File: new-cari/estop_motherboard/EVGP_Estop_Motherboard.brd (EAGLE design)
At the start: 82.6 x 94.1 mm, 45 parts, among them J1 JST-XH-02-PIN-LONG-PAD, J2 JST-XH-02-PIN-LONG-PAD, J3 JST-XH-03-PIN-LONG-PAD, J4 JST-XH-03-PIN-LONG-PAD, J5 AVR_SPI_PROG_3X2PTH, J6 UX60-MB-5S8, J7 JST-XH-04-PIN-LONG-PAD, J8 JST-XH-03-PIN-LONG-PAD, J9 JST-XH-02-PIN-LONG-PAD, Q1 NFETS_1, Q2 N_FETS2, U1 ATMEGA32U4-AU, U2 NL27WZ08USG, U3 NL27WZ08USG, X1 TSX-3225 16.0000MF18X-AC0

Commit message: test
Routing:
- net PUSH_BUTTON: track 32.5 -> 28.5 mm
- net STEERING_EN_OUT: track 28.5 -> 26.2 mm
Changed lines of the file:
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@@
 <?xml version="1.0" encoding="utf-8"?>
 <!DOCTYPE eagle SYSTEM "eagle.dtd">
-<eagle version="9.5.0">
+<eagle version="9.5.1">
 <drawing>
 <settings>
-<setting alwaysvectorfont="no"/>
+<setting alwaysvectorfont="yes"/>
 <setting verticaltext="up"/>
 </settings>
@@
 <wire x1="66.1966" y1="7.08" x2="68" y2="8.8834" width="0.2032" layer="1"/>
 <via x="68" y="8.8834" extent="1-16" drill="0.508"/>
-<via x="72.022303125" y="11.922303125" extent="1-16" drill="0.508"/>
-<wire x1="68" y1="8.8834" x2="71.038903125" y2="11.922303125" width="0.2032" layer="16"/>
-<wire x1="71.038903125" y1="11.922303125" x2="72.022303125" y2="11.922303125" width="0.2032" layer="16"/>
+<via x="72.622303125" y="11.722303125" extent="1-16" drill="0.508"/>
+<wire x1="68" y1="8.8834" x2="70.838903125" y2="11.722303125" width="0.2032" layer="16"/>
+<wire x1="70.838903125" y1="11.722303125" x2="72.622303125" y2="11.722303125" width="0.2032" layer="16"/>
 <wire x1="76.9224" y1="9.25" x2="76.31118125" y2="9.25" width="0.2032" layer="1"/>
-<wire x1="73.638878125" y1="11.922303125" x2="72.022303125" y2="11.922303125" width="0.2032" layer="1"/>
-<wire x1="76.31118125" y1="9.25" x2="73.638878125" y2="11.922303125" width="0.2032" layer="1"/>
+<wire x1="73.838878125" y1="11.722303125" x2="72.622303125" y2="11.722303125" width="0.2032" layer="1"/>
+<wire x1="76.31118125" y1="9.25" x2="73.838878125" y2="11.722303125" width="0.2032" layer="1"/>
 </signal>
 <signal name="STEERING_EN_RB">
@@
 <wire x1="80.5" y1="17.95" x2="81.65" y2="19.1" width="0.2032" layer="1"/>
 <wire x1="80.5" y1="11.79746875" x2="80.5" y2="17.95" width="0.2032" layer="1"/>
-<wire x1="80.55" y1="22.05" x2="80.55" y2="20.2" width="0.2032" layer="1"/>
-<wire x1="81.65" y1="19.1" x2="80.55" y2="20.2" width="0.2032" layer="1"/>
-<wire x1="81.5" y1="23" x2="86" y2="23" width="0.2032" layer="1"/>
-<wire x1="86" y1="23" x2="87" y2="24" width="0.2032" layer="1"/>
-<wire x1="87" y1="26.5" x2="85.53" y2="27.97" width="0.2032" layer="1"/>
+<wire x1="86.5" y1="27" x2="86.5" y2="23.95" width="0.2032" layer="1"/>
+<wire x1="81.65" y1="19.1" x2="86.5" y2="23.95" width="0.2032" layer="1"/>
+<wire x1="86.5" y1="27" x2="85.53" y2="27.97" width="0.2032" layer="1"/>
 <wire x1="85.53" y1="27.97" x2="84.4" y2="27.97" width="0.2032" layer="1"/>
-<wire x1="80.55" y1="22.05" x2="81.5" y2="23" width="0.2032" layer="1"/>
-<wire x1="87" y1="24" x2="87" y2="26.5" width="0.2032" layer="1"/>
 </signal>
 <signal name="DRIVE_EN_OUT">
@@
 <contactref element="U2" pad="3"/>
 <contactref element="J1" pad="1"/>
-<wire x1="84.5" y1="1.23" x2="80.77" y2="1.23" width="0.2032" layer="1"/>
-<wire x1="80" y1="6" x2="79.5" y2="6.5" width="0.2032" layer="1"/>
-<wire x1="80.77" y1="1.23" x2="80" y2="2" width="0.2032" layer="1"/>
-<wire x1="80" y1="2" x2="80" y2="6" width="0.2032" layer="1"/>
+<wire x1="84.5" y1="1.23" x2="78.07" y2="1.23" width="0.2032" layer="1"/>
+<wire x1="78.07" y1="1.23" x2="71.3" y2="8" width="0.2032" layer="1"/>
 <wire x1="70.2" y1="10.46118125" x2="70.2" y2="13.2" width="0.2032" layer="1"/>
 <via x="70.2" y="13.2" extent="1-16" drill="0.508"/>
-<wire x1="72.8" y1="6.5" x2="71.3" y2="8" width="0.2032" layer="1"/>
 <wire x1="71.3" y1="8" x2="71.3" y2="9.4" width="0.2032" layer="1"/>
 <wire x1="71.3" y1="9.4" x2="70.2" y2="10.46118125" width="0.2032" layer="1"/>
@@
 <wire x1="74.0776" y1="14.75" x2="71.905390625" y2="14.75" width="0.2032" layer="1"/>
 <wire x1="71.877696875" y1="14.722303125" x2="71.905390625" y2="14.75" width="0.2032" layer="1"/>
-<wire x1="79.5" y1="6.5" x2="72.8" y2="6.5" width="0.2032" layer="1"/>
 </signal>
 <signal name="STEERING_EN_IN">

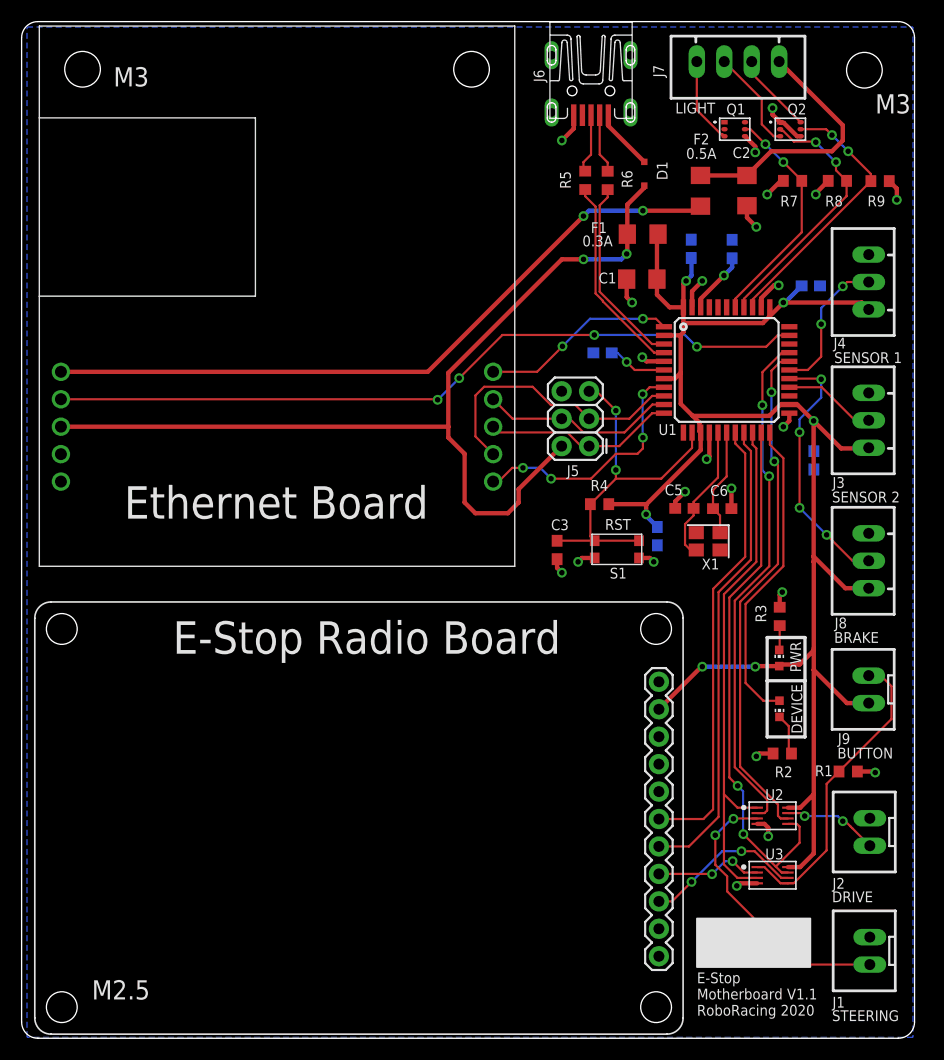
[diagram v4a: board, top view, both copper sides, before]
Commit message: updated ethernet poe board, made some minor rerouting changes, and cleaned everything up a bit
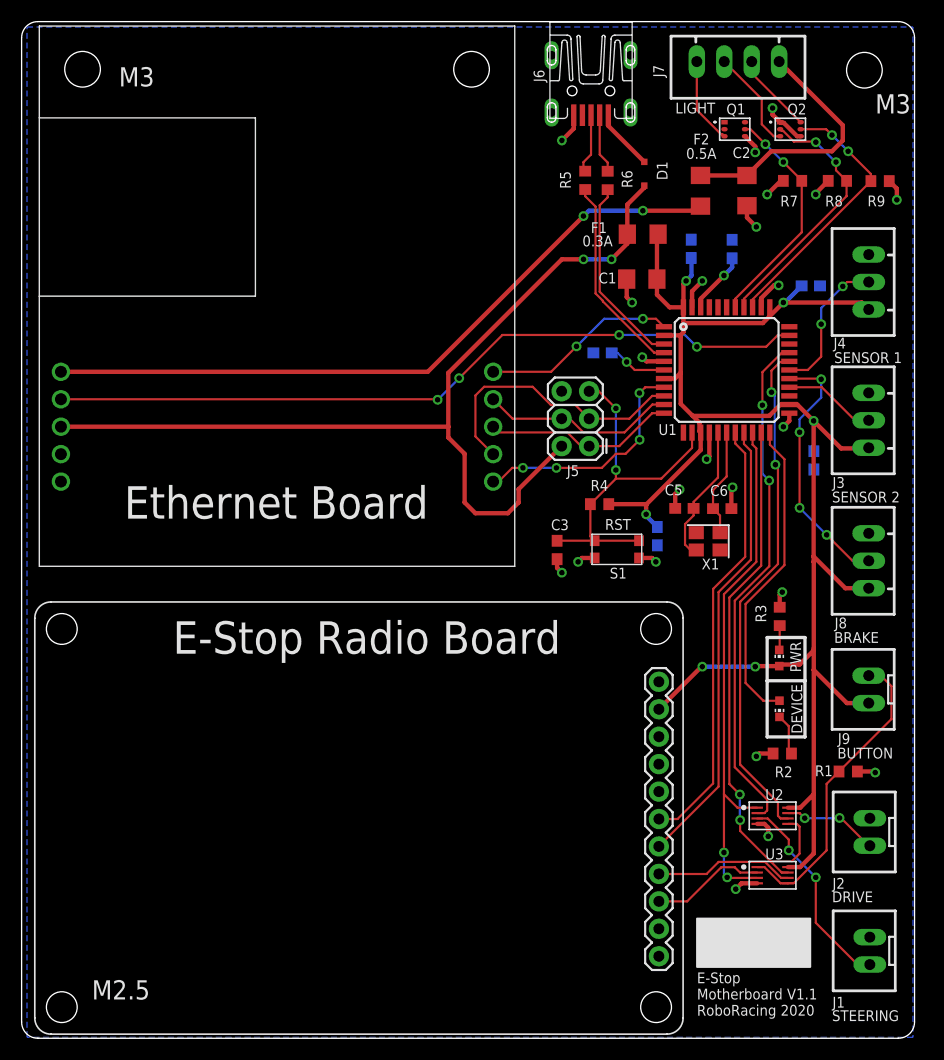
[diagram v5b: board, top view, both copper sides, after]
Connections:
- net DRIVE_EN_RB: now also U3.2; no longer U3.6
- net STEERING_EN_RB: now also U3.6; no longer U3.2
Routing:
- net STEERING_EN_OUT: track 26.2 -> 19.1 mm
- net DRIVE_EN_RB: track 14.9 -> 10.6 mm, vias 2 -> 0
- net STEERING_EN_RB: track 10.0 -> 13.0 mm, vias 2 -> 0
- net START_RB: track 43.7 -> 42.1 mm
- net SAFE_RB: track 41.9 -> 40.5 mm
- net SS: track 23.2 -> 22.0 mm
- net DRIVE_EN_IN: track 50.3 -> 51.2 mm
- net GND: track 48.4 -> 49.0 mm
- net STEERING_EN_IN: track 48.5 -> 49.1 mm, vias 0 -> 2
- net 5V_UNFUSED: track 89.2 -> 88.7 mm

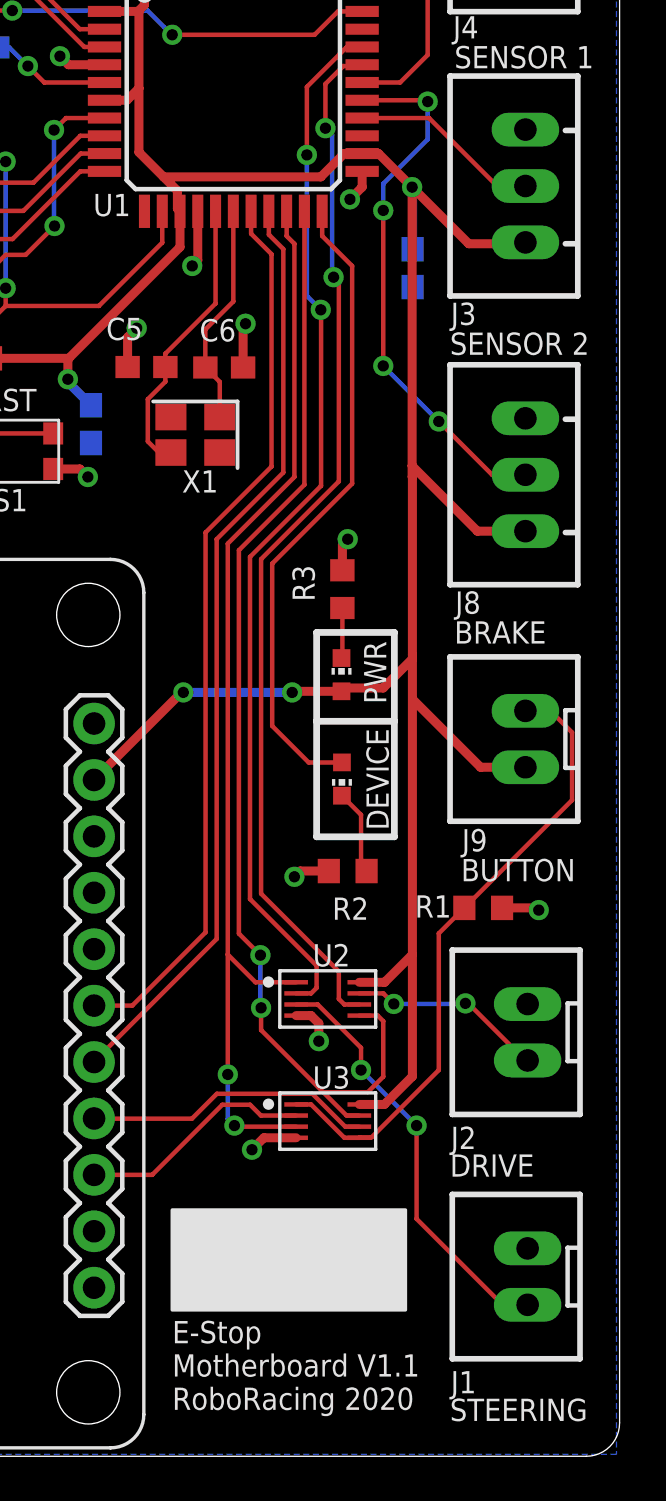
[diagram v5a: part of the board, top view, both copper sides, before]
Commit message: moved LED1 to pin 25
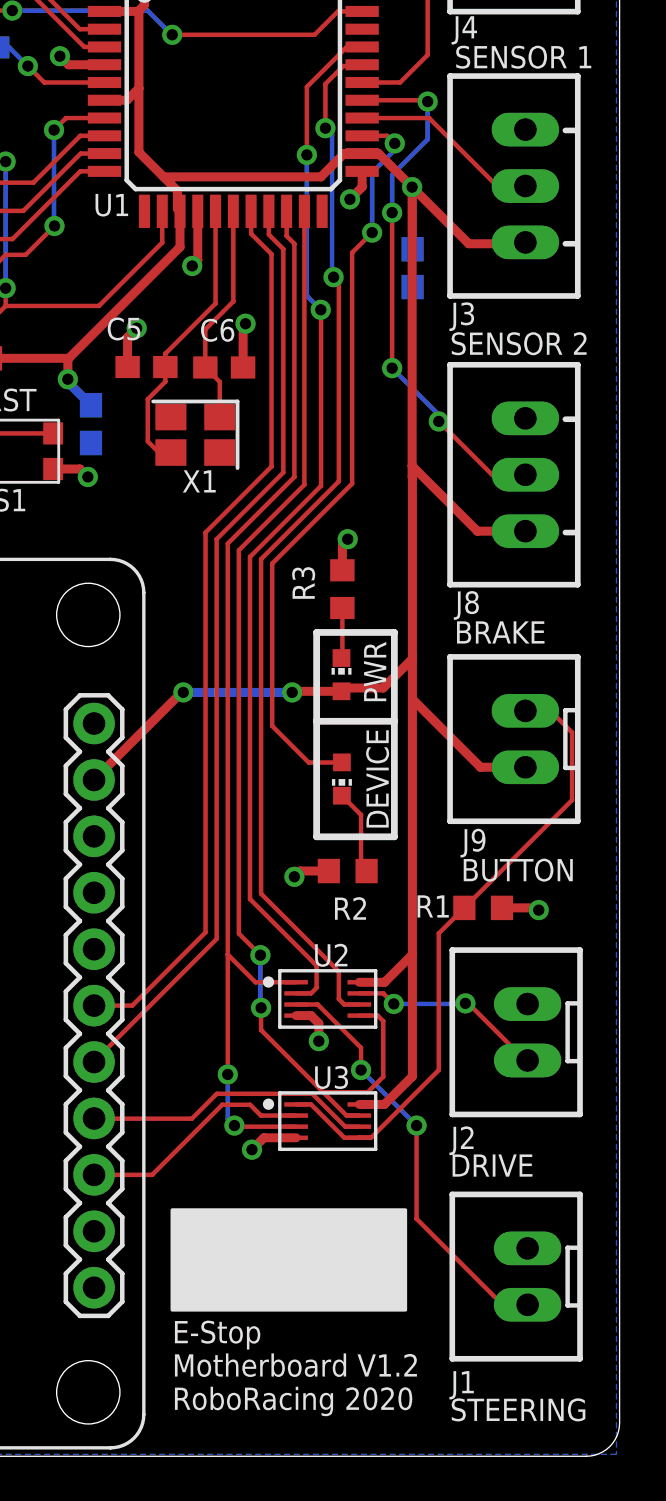
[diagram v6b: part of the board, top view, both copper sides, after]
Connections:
- net LED1: now also U1.25; no longer U1.22
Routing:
- net LED1: track 29.0 -> 33.9 mm, vias 0 -> 2
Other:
- board text added: "E-Stop Motherboard V1.2 RoboRacing 2020"
- board text removed: "E-Stop Motherboard V1.1 RoboRacing 2020"
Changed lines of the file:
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@@
 <drawing>
 <settings>
-<setting alwaysvectorfont="yes"/>
+<setting alwaysvectorfont="no"/>
 <setting verticaltext="up"/>
 </settings>
@@
 <text x="67.5" y="75.8" size="1" layer="21" font="vector">0.5A</text>
 <text x="68.5" y="-3.5" size="1" layer="21" font="vector">E-Stop
-Motherboard V1.1
+Motherboard V1.2
 RoboRacing 2020</text>
 <polygon width="0.1524" layer="21">
@@
 <signal name="LED1">
 <contactref element="DEVICE" pad="A"/>
-<contactref element="U1" pad="22"/>
-<wire x1="75.25" y1="49.35" x2="75.25" y2="50.46" width="0.2032" layer="1"/>
 <wire x1="73" y1="27.29" x2="73" y2="34.6" width="0.2032" layer="1"/>
-<wire x1="73" y1="34.6" x2="76.6" y2="38.2" width="0.2032" layer="1"/>
-<wire x1="76.6" y1="38.2" x2="76.6" y2="48" width="0.2032" layer="1"/>
-<wire x1="76.6" y1="48" x2="75.25" y2="49.35" width="0.2032" layer="1"/>
+<wire x1="76.6" y1="38.2" x2="73" y2="34.6" width="0.2032" layer="1"/>
 <wire x1="74.645" y1="25.645" x2="73" y2="27.29" width="0.2032" layer="1"/>
 <wire x1="74.645" y1="25.645" x2="76.135" y2="25.645" width="0.2032" layer="1"/>
 <wire x1="76.135" y1="25.645" x2="76.14" y2="25.65" width="0.2032" layer="1"/>
+<contactref element="U1" pad="25"/>
+<wire x1="77.05" y1="53.86" x2="78.1742125" y2="53.86" width="0.2032" layer="1"/>
+<wire x1="78.1742125" y1="53.86" x2="78.51710625" y2="53.51710625" width="0.2032" layer="1"/>
+<via x="78.51710625" y="53.51710625" extent="1-16" drill="0.508"/>
+<wire x1="78.51710625" y1="53.51710625" x2="78.51710625" y2="53.21710625" width="0.2032" layer="16"/>
+<wire x1="77.5" y1="52.2" x2="77.5" y2="49.5" width="0.2032" layer="16"/>
+<via x="77.5" y="49.5" extent="1-16" drill="0.508"/>
+<wire x1="77.5" y1="49.5" x2="76.6" y2="48.6" width="0.2032" layer="1"/>
+<wire x1="78.51710625" y1="53.21710625" x2="77.5" y2="52.2" width="0.2032" layer="16"/>
+<wire x1="76.6" y1="48.6" x2="76.6" y2="38.2" width="0.2032" layer="1"/>
 </signal>
 <signal name="STACK_MCU1">
@@
 <signal name="BRAKE_EN">
 <contactref element="J8" pad="2"/>
-<via x="78" y="43.5" extent="1-16" drill="0.508"/>
-<wire x1="78" y1="43.5" x2="78" y2="50.5" width="0.2032" layer="1"/>
-<via x="78" y="50.5" extent="1-16" drill="0.508"/>
+<via x="78.4" y="43.4" extent="1-16" drill="0.508"/>
+<wire x1="78.4" y1="50.4" x2="78.4" y2="43.4" width="0.2032" layer="1"/>
+<via x="78.4" y="50.4" extent="1-16" drill="0.508"/>
 <via x="80" y="55.4" extent="1-16" drill="0.508"/>
 <wire x1="80" y1="55.4" x2="80" y2="53.7" width="0.2032" layer="16"/>
-<wire x1="80" y1="53.7" x2="78" y2="51.7" width="0.2032" layer="16"/>
-<wire x1="78" y1="51.7" x2="78" y2="50.5" width="0.2032" layer="16"/>
-<wire x1="80.5" y1="41" x2="78" y2="43.5" width="0.2032" layer="16"/>
+<wire x1="80" y1="53.7" x2="78.4" y2="52.1" width="0.2032" layer="16"/>
+<wire x1="78.4" y1="52.1" x2="78.4" y2="50.4" width="0.2032" layer="16"/>
+<wire x1="80.5" y1="41" x2="80.5" y2="41.3" width="0.2032" layer="16"/>
+<wire x1="80.5" y1="41.3" x2="78.4" y2="43.4" width="0.2032" layer="16"/>
 <via x="80.5" y="41" extent="1-16" drill="0.508"/>
 <wire x1="82.9" y1="38.6" x2="80.5" y2="41" width="0.2032" layer="1"/>
